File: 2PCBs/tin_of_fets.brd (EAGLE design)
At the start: 58.4 x 55.9 mm, 59 parts, among them J4 PJ-040X, Q1 J112, Q2 J112, Q3 ZVN4306A, Q4 ZVN4306A, Q5 ZTX694B, Q6 J112, Q7 J112, Q8 ZVN4306A, Q9 ZVN4306A

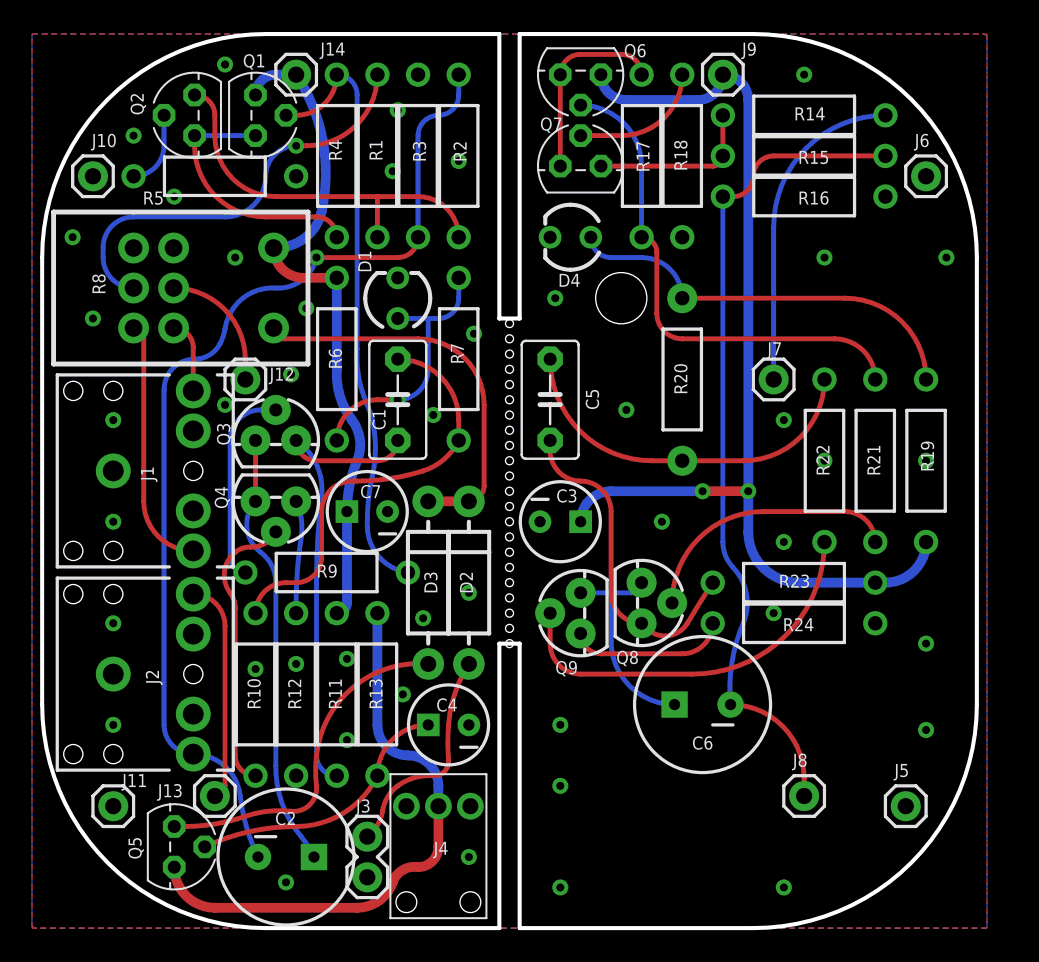
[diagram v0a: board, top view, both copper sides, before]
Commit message: Li-ion powered version WIP
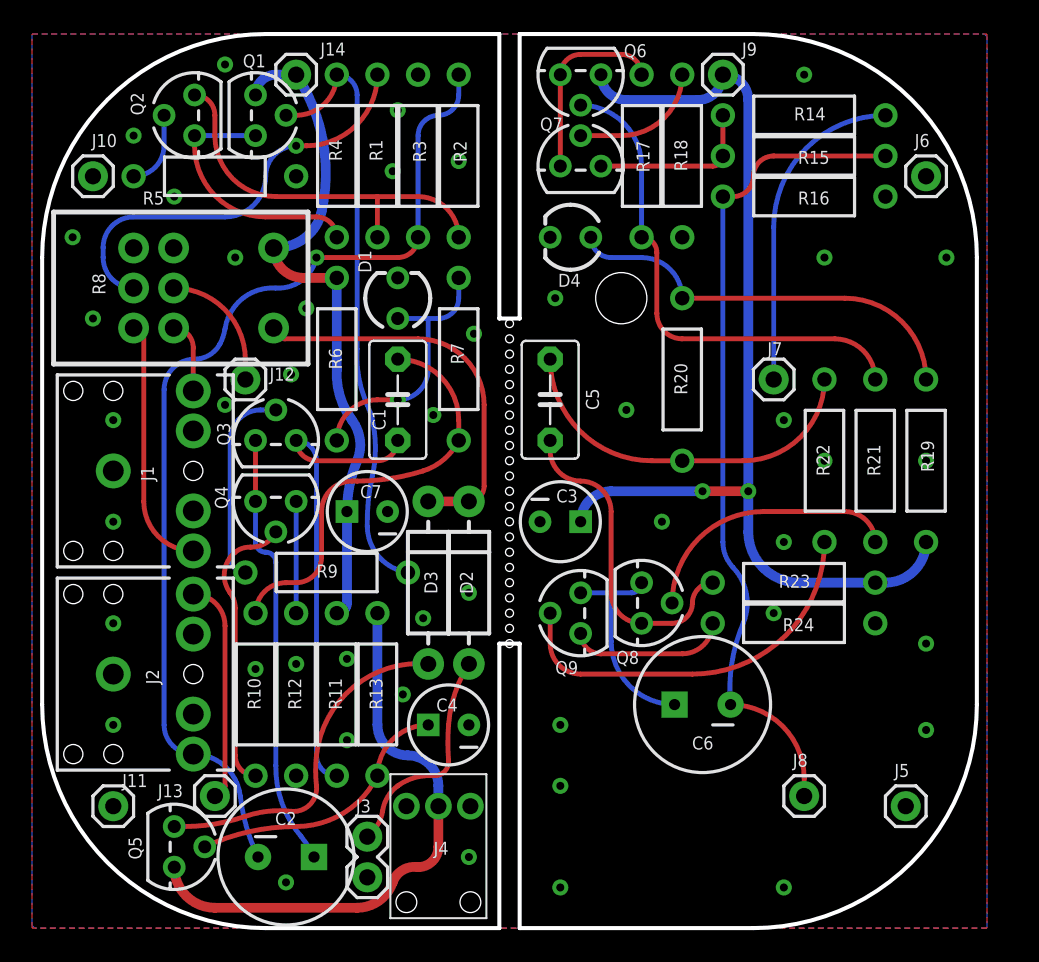
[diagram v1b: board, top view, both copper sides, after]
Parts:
- Q1, Q2, Q6, Q7: device transistor-fet:TO92 -> my-tran:TO-92
- Q3, Q4, Q8, Q9: device SparkFun-DiscreteSemi:TO-92 -> my-tran:TO-92
- Q5: device my-tran:TO92 -> my-tran:TO-92
- R20: device my-res:AXIAL-0.4 -> my-res:AXIAL-0.4-SM
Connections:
- net +12V: now also Q5.3; no longer Q5.1
- net N$15: now also Q7.3; no longer Q7.1
- net N$2: now also Q1.3, Q2.1; no longer Q1.1, Q2.3
- net N$23: now also Q5.1; no longer Q5.3
- net N$6: now also Q2.3; no longer Q2.1
- net N$7: now also Q6.3, Q7.1; no longer Q6.1, Q7.3
- net VCC: now also Q1.1, Q6.1; no longer Q1.3, Q6.3
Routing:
- net N$20: track 19.8 -> 19.3 mm

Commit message: Stamp holes removed
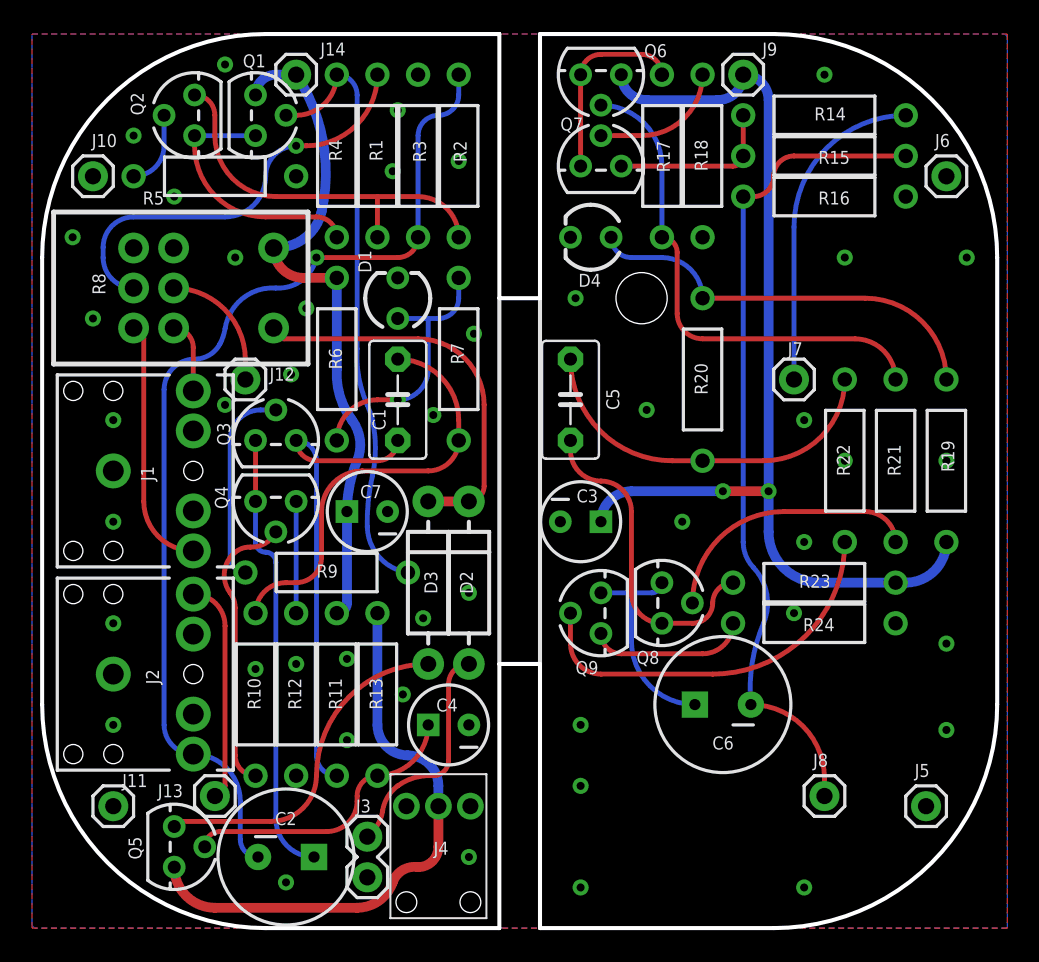
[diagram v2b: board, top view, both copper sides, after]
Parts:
- moved C5 1.27 mm to (33.7, 33.0)
- moved C6 1.27 mm to (43.2, 14.0)
- moved J5 1.27 mm to (55.9, 7.62)
- moved J7 1.27 mm to (47.6, 34.3)
- moved J8 1.27 mm to (49.5, 8.26)
- moved J9 1.27 mm to (44.5, 53.3)
- moved LOGO1 1.27 mm to (40.6, 7.62)
- moved Q6 1.27 mm to (35.6, 53.3)
- moved Q7 1.27 mm to (35.6, 47.6)
- moved Q9 1.27 mm to (35.6, 19.7)
- moved R14 1.27 mm to (49.5, 50.8)
- moved R15 1.27 mm to (49.5, 48.3)
- moved R16 1.27 mm to (49.5, 45.7)
- moved R21 1.27 mm to (54.0, 29.2)
- moved R23 1.27 mm to (48.9, 21.6)
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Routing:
- net N$24: track 16.3 -> 17.3 mm
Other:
- board size 58.4 x 55.9 mm -> 59.7 x 55.9 mm
- board text added: "Portuum"

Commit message: Small improvements
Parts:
- removed J11, J6: (no value), SparkFun-Connectors:1X01
- added D5: 1N4148, SparkFun-DiscreteSemi:DIODE-1N4148
- D2, D3: value (none) -> 1N5819-B; device SparkFun-DiscreteSemi:DIODE-1N4001 -> diode:DO41-7.6
- moved J5 39.4 mm to (57.1, 47.0)
- moved J13 6.25 mm to (5.71, 5.71)
- moved J8 6.25 mm to (55.2, 5.71)
- moved Q5 0.63 mm to (8.89, 4.45)
- turned D2 to 270 degrees
- turned D3 to 270 degrees
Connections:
- net +12V: now also D5.C
- net GND: no longer J11.1, J6.1
- net N$23: now also D5.A
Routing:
- net OUT_R: track 64.5 -> 73.9 mm
- net N$23: track 20.1 -> 27.7 mm
- net +12V: track 35.0 -> 42.4 mm
- net VCC*: track 24.1 -> 25.4 mm
- net VBAT: track 13.9 -> 15.2 mm
